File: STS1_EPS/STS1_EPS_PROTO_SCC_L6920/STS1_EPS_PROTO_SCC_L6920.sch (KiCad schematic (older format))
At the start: 15 parts, among them J1 Screw_Terminal_01x02, J2 Screw_Terminal_01x02, Q1 2N7000

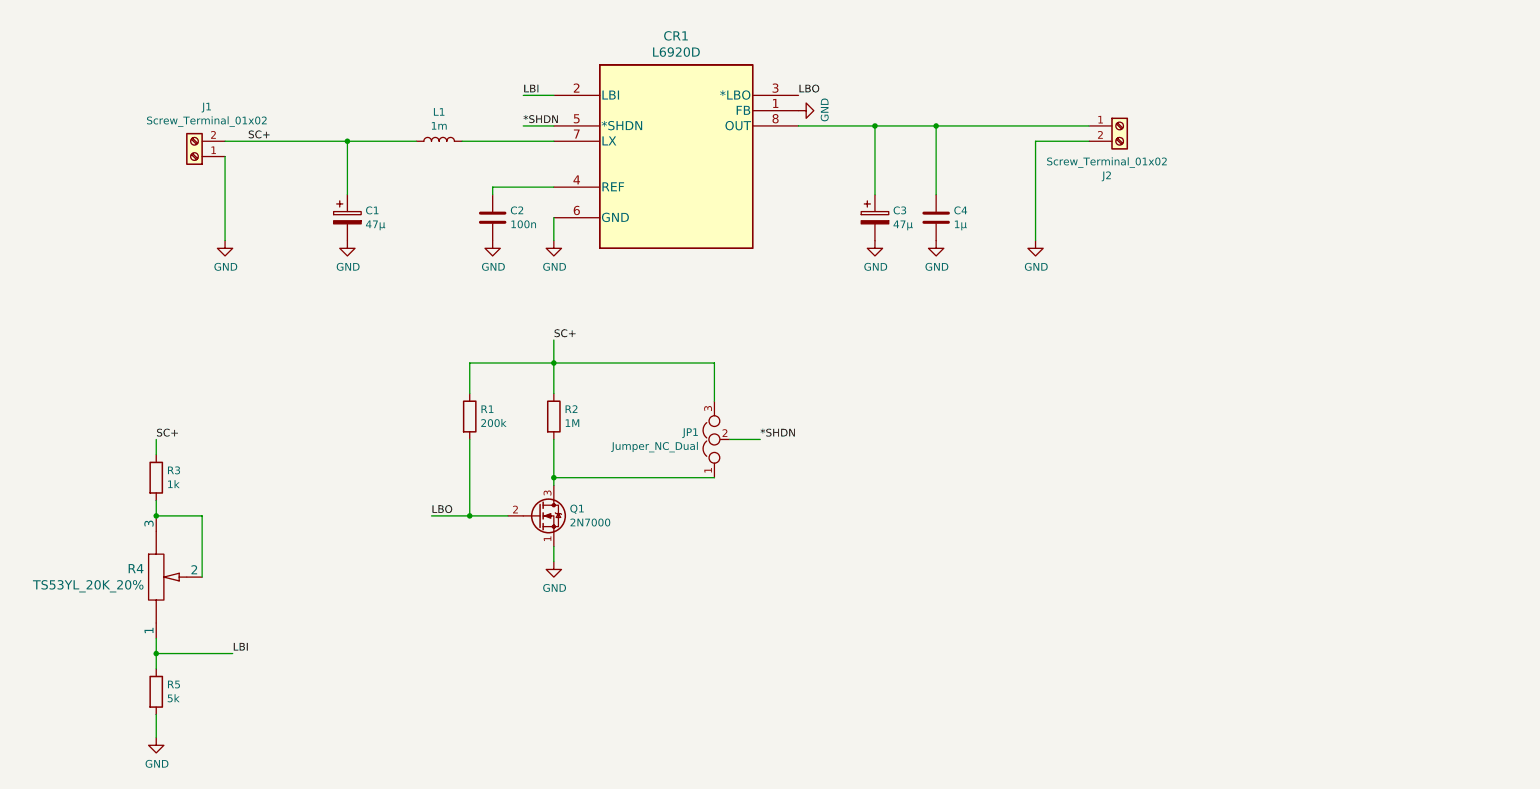
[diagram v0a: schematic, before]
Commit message: - STS1_EPS_PROTO_SCC_L6920 now uses the STS1 PCB template and is again ready for review. - WOrked on STS1_EPS_PROTO_BCC_LTC4020.
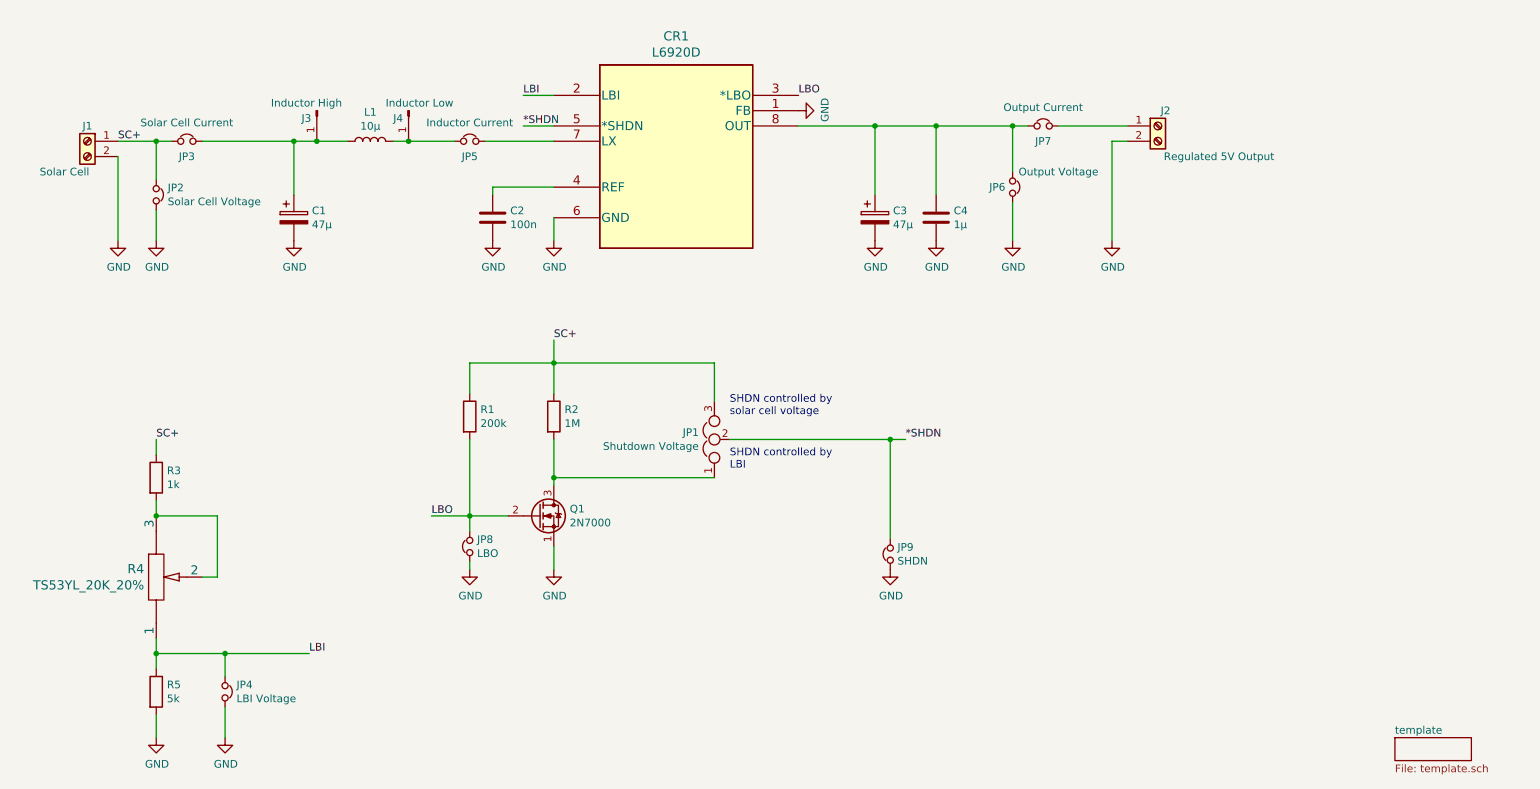
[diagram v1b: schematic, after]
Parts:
- added J3: Inductor High, Connector_PinSocket_2.54mm:PinSocket_1x01_P2.54mm_Vertical, symbol Connector:Conn_01x01_Male
- added J4: Inductor Low, Connector_PinSocket_2.54mm:PinSocket_1x01_P2.54mm_Vertical, symbol Connector:Conn_01x01_Male
- added JP2: Solar Cell Voltage, Connector_PinSocket_2.54mm:PinSocket_1x02_P2.54mm_Vertical, symbol Device:Jumper_NC_Small
- added JP3: Solar Cell Current, Connector_PinSocket_2.54mm:PinSocket_1x02_P2.54mm_Vertical, symbol Device:Jumper_NC_Small
- added JP4: LBI Voltage, Connector_PinSocket_2.54mm:PinSocket_1x02_P2.54mm_Vertical, symbol Device:Jumper_NC_Small
- added JP5: Inductor Current, Connector_PinSocket_2.54mm:PinSocket_1x02_P2.54mm_Vertical, symbol Device:Jumper_NC_Small
- added JP6: Output Voltage, Connector_PinSocket_2.54mm:PinSocket_1x02_P2.54mm_Vertical, symbol Device:Jumper_NC_Small
- added JP7: Output Current, Connector_PinSocket_2.54mm:PinSocket_1x02_P2.54mm_Vertical, symbol Device:Jumper_NC_Small
- added JP8: LBO, Connector_PinSocket_2.54mm:PinSocket_1x02_P2.54mm_Vertical, symbol Device:Jumper_NC_Small
- added JP9: SHDN, Connector_PinSocket_2.54mm:PinSocket_1x02_P2.54mm_Vertical, symbol Device:Jumper_NC_Small
- J1: value Screw_Terminal_01x02 -> Solar Cell
- J2: value Screw_Terminal_01x02 -> Regulated 5V Output
- JP1: value Jumper_NC_Dual -> Shutdown Voltage
- L1: value 1m -> 10µ; footprint Inductor_THT:L_Axial_L5.3mm_D2.2mm_P10.16mm_Horizontal_Vishay_IM-1 -> footprints:DO1608C-103C
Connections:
- net *SHDN: now also JP9.2
- net GND: now also J1.2 (Pin_2), JP2.2, JP4.2, JP6.2, JP8.1, JP9.1; no longer J1.1 (Pin_1)
- net LBI: now also JP4.1
- net LBO: now also JP8.2
- net SC+: now also J1.1 (Pin_1), JP2.1, JP3.1; no longer C1.1, J1.2 (Pin_2), L1.1
- net at C3.1, C4.1, CR1.8 (OUT): now also JP6.1, JP7.1; no longer J2.1 (Pin_1)
- net at CR1.7 (LX): now also JP5.2; no longer L1.2
- new net: C1.1, J3.1 (Pin_1), JP3.2, L1.1
- new net: J4.1 (Pin_1), JP5.1, L1.2
- new net: J2.1 (Pin_1), JP7.2
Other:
- note added: "SHDN controlled by\nLBI"
- note added: "SHDN controlled by\nsolar cell voltage"
- moved on the sheet: C1, J1, J2, L1

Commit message: Incorporated feedback into BCC and SCC - Fixed "unspecified" pin type warnings - Added correct test point symbols - Added thermal blockers - Added DRC parameters and fixed DRC issues - Adapted CubeSat STS1 PCB template to not violate DRC
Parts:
- J3, J4: symbol Connector:Conn_01x01_Male -> Connector:TestPoint
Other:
- moved on the sheet: L1
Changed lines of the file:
@@
 F 1 "L6920D" H 5650 2181 60  0000 C CNN
 F 2 "footprints:L6920D" H 5650 2140 60  0001 C CNN
-F 3 "" H 4850 1900 60  0000 C CNN
+F 3 "https://www.st.com/resource/en/datasheet/l6920.pdf" H 4850 1900 60  0001 C CNN
 	1    4850 1900
 	1    0    0    -1
@@
 L Device:L L?
 U 1 1 60DA1D0F
-P 3650 2200
+P 3600 2200
 AR Path="/60DA6FCF/60DA1D0F" Ref="L?"  Part="1"
 AR Path="/60DA7492/60DA1D0F" Ref="L?"  Part="1"
@@
 AR Path="/60DA84E4/60DA1D0F" Ref="L?"  Part="1"
 AR Path="/60DA1D0F" Ref="L1"  Part="1"
-F 0 "L1" V 3840 2200 50  0000 C CNN
-F 1 "10µ" V 3749 2200 50  0000 C CNN
-F 2 "footprints:DO1608C-103C" H 3650 2200 50  0001 C CNN
-F 3 "https://www.mouser.at/datasheet/2/597/do1608c-270726.pdf" H 3650 2200 50  0001 C CNN
-	1    3650 2200
+F 0 "L1" V 3790 2200 50  0000 C CNN
+F 1 "10µ" V 3699 2200 50  0000 C CNN
+F 2 "footprints:DO1608C-103C" H 3600 2200 50  0001 C CNN
+F 3 "https://www.mouser.at/datasheet/2/597/do1608c-270726.pdf" H 3600 2200 50  0001 C CNN
+	1    3600 2200
 	0    -1   -1   0
 $EndComp
@@
 	4850 2200 4400 2200
 Wire Wire Line
-	3500 2200 3300 2200
+	3450 2200 3300 2200
 Wire Wire Line
 	3150 2200 3150 2550
@@
 SHDN controlled by\nLBI
 $Comp
-L Connector:Conn_01x01_Male J3
+L Connector:TestPoint J3
 U 1 1 60E2457A
-P 3300 2000
-F 0 "J3" V 3350 1900 50  0000 L CNN
-F 1 "Inductor High" V 3250 1700 50  0000 L CNN
-F 2 "Connector_PinSocket_2.54mm:PinSocket_1x01_P2.54mm_Vertical" H 3300 2000 50  0001 C CNN
-F 3 "~" H 3300 2000 50  0001 C CNN
-	1    3300 2000
-	0    1    1    0
+P 3300 2200
+F 0 "J3" H 3150 2350 50  0000 L CNN
+F 1 "Inductor High" V 3300 2400 50  0000 L CNN
+F 2 "Connector_PinSocket_2.54mm:PinSocket_1x01_P2.54mm_Vertical" H 3300 2200 50  0001 C CNN
+F 3 "~" H 3300 2200 50  0001 C CNN
+	1    3300 2200
+	1    0    0    -1
 $EndComp
 Connection ~ 3300 2200
@@
 	3300 2200 3150 2200
 $Comp
-L Connector:Conn_01x01_Male J4
+L Connector:TestPoint J4
 U 1 1 60E2512B
-P 3900 2000
-F 0 "J4" V 3950 1900 50  0000 L CNN
-F 1 "Inductor Low" V 3850 1850 50  0000 L CNN
-F 2 "Connector_PinSocket_2.54mm:PinSocket_1x01_P2.54mm_Vertical" H 3900 2000 50  0001 C CNN
-F 3 "~" H 3900 2000 50  0001 C CNN
-	1    3900 2000
-	0    1    1    0
+P 3900 2200
+F 0 "J4" H 3750 2350 50  0000 L CNN
+F 1 "Inductor Low" V 3900 2400 50  0000 L CNN
+F 2 "Connector_PinSocket_2.54mm:PinSocket_1x01_P2.54mm_Vertical" H 3900 2200 50  0001 C CNN
+F 3 "~" H 3900 2200 50  0001 C CNN
+	1    3900 2200
+	1    0    0    -1
 $EndComp
 Connection ~ 3900 2200
 Wire Wire Line
-	3900 2200 3800 2200
+	3900 2200 3750 2200
 $Comp
 L Device:Jumper_NC_Small JP8

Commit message: Replaced electrolyte capacitors of SCC with tantalum capacitors.
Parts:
- C1, C3: Part. Nr. (none) -> F380K476MSA
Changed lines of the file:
@@
 F 1 "47µ" H 3268 2655 50  0000 L CNN
 F 2 "Capacitor_SMD:C_0805_2012Metric" H 3188 2550 50  0001 C CNN
-F 3 "~" H 3150 2700 50  0001 C CNN
+F 3 "https://www.mouser.at/datasheet/2/40/F38-2400651.pdf" H 3150 2700 50  0001 C CNN
+F 4 "F380K476MSA" H 3150 2700 50  0001 C CNN "Part. Nr."
 	1    3150 2700
 	1    0    0    -1
@@
 F 1 "47µ" H 7068 2655 50  0000 L CNN
 F 2 "Capacitor_SMD:C_0805_2012Metric" H 6988 2550 50  0001 C CNN
-F 3 "~" H 6950 2700 50  0001 C CNN
+F 3 "https://www.mouser.at/datasheet/2/40/F38-2400651.pdf" H 6950 2700 50  0001 C CNN
+F 4 "F380K476MSA" H 6950 2700 50  0001 C CNN "Part. Nr."
 	1    6950 2700
 	1    0    0    -1
